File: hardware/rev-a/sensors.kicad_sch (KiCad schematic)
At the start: 14 parts, among them J4 SOIL, Q3 AO3401A, U5 BME280

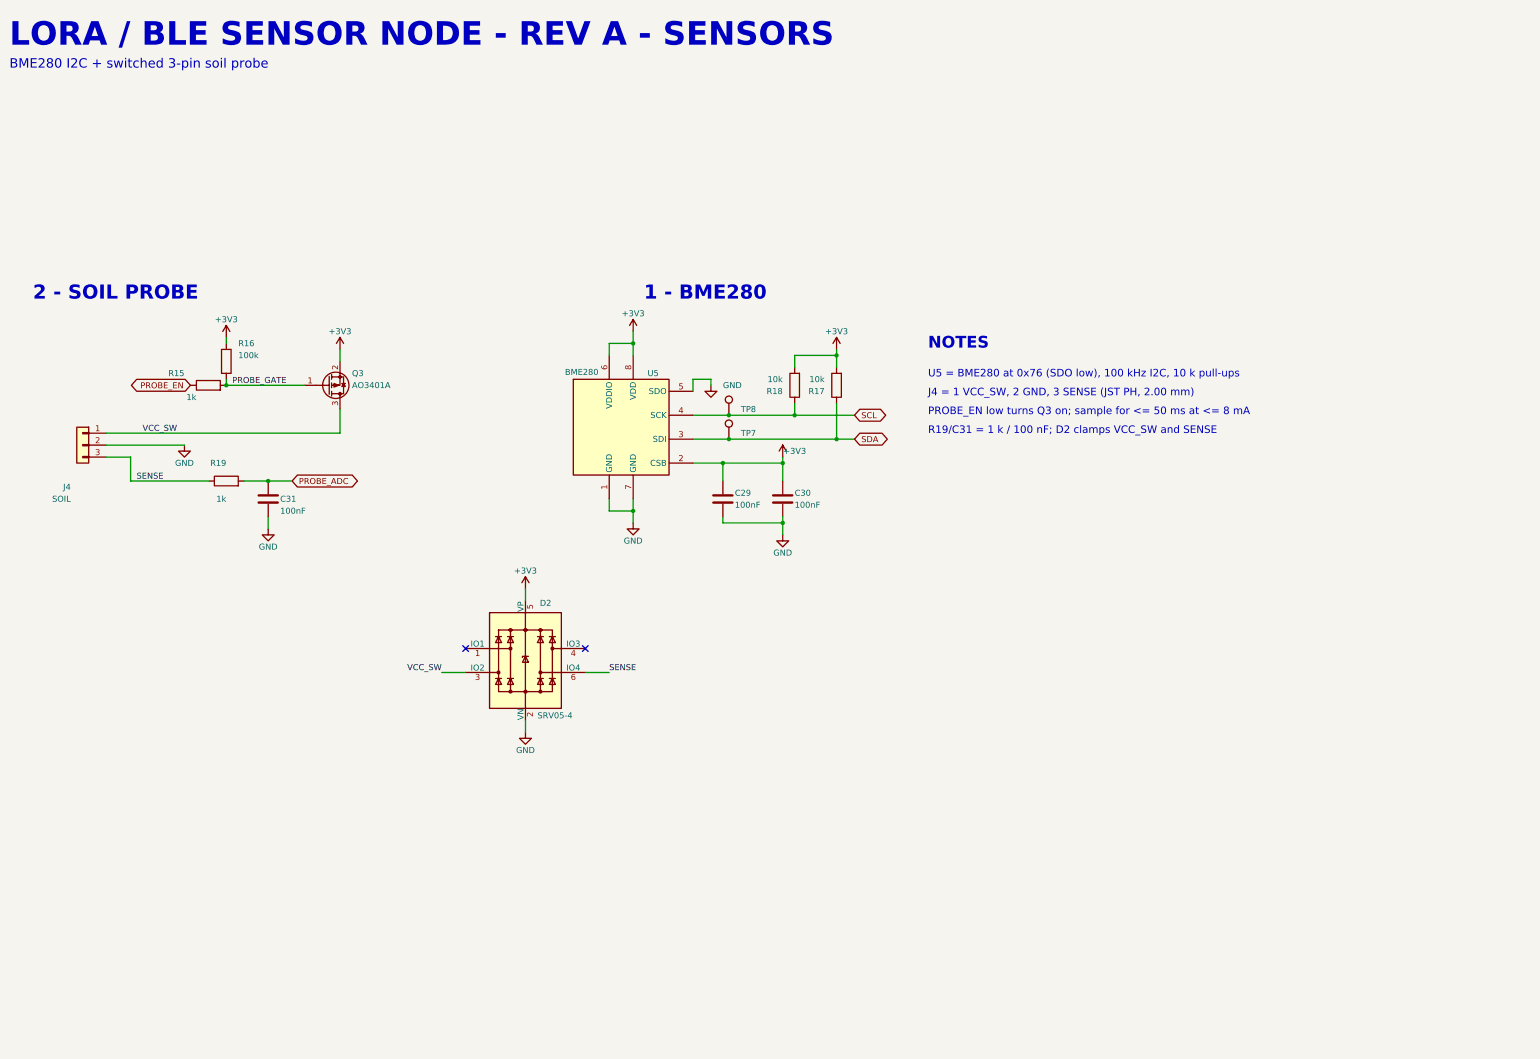
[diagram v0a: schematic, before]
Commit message: Schematic: cosmetic pass over the sheet artwork
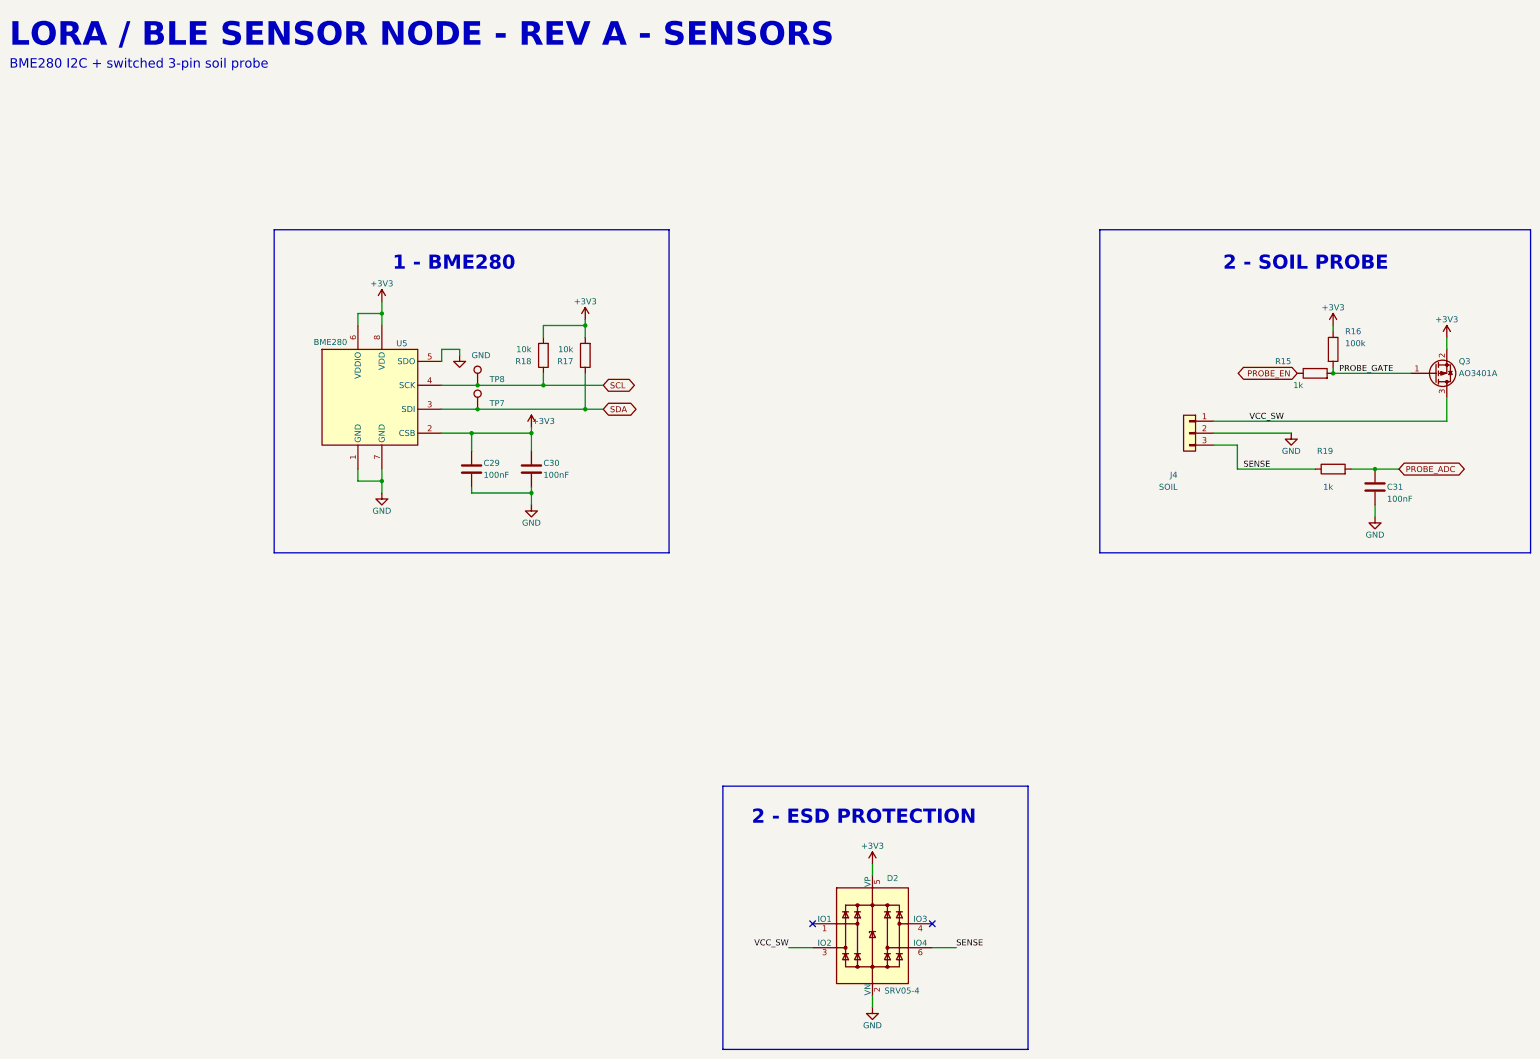
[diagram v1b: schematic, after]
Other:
- note added: "2 - ESD PROTECTION"
- note removed: "J4 = 1 VCC_SW, 2 GND, 3 SENSE (JST PH, 2.00 mm)"
- note removed: "NOTES"
- note removed: "PROBE_EN low turns Q3 on; sample for <= 50 ms at <= 8 mA"
- note removed: "R19/C31 = 1 k / 100 nF; D2 clamps VCC_SW and SENSE"
- note removed: "U5 = BME280 at 0x76 (SDO low), 100 kHz I2C, 10 k pull-ups"
- moved on the sheet: C29, C30, C31, D2, J4, Q3, R15, R16, R17, R18, R19, TP7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
